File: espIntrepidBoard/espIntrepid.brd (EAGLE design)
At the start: 64 x 56 mm, 23 parts, among them Q1 TRANS_NPN, Q7 TRANS_NPN, U1 ESP32DEV_38, U2 MOSFET_P, U3 LTV-847, U5 SN65HVD233D, U6 LTV-817

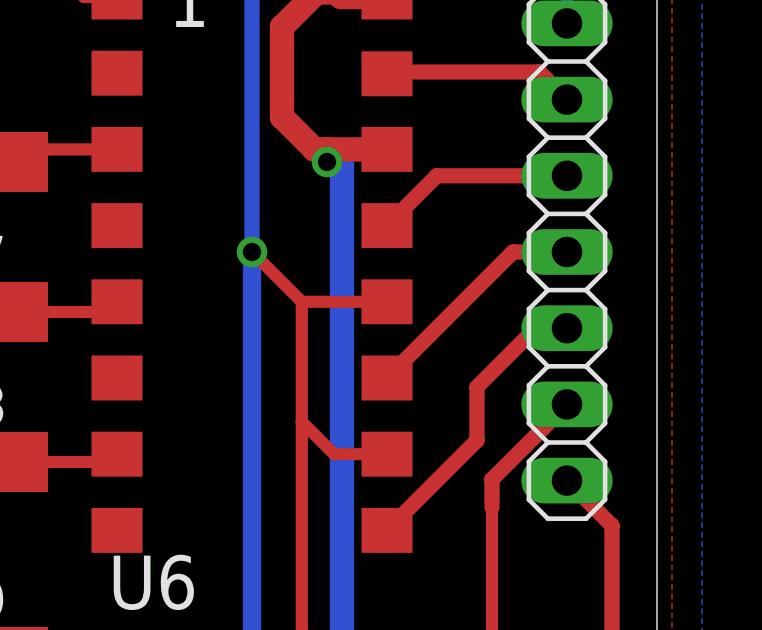
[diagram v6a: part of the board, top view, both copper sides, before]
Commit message: -Swapped 2 pins on board -Added reverse engg schematic
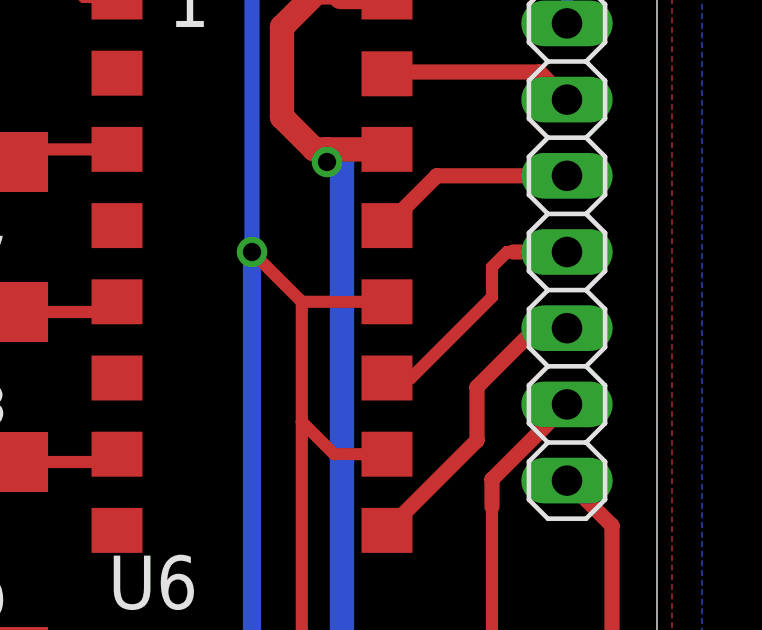
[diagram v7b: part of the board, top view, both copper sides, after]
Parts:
- Q1: value TRANS_NPN -> C1815
- R1: value (none) -> 5.6k
- R10: value (none) -> 1800
- R4: value (none) -> 5.6K
- R5, R6, R7, R8, R9: value (none) -> 470
- U2: value MOSFET_P -> DMG2307
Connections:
- net ABS: now also JP6.4, U3.11; no longer JP6.5, U3.9
- net ABS_UC: now also R7.1, U1.31; no longer R8.1, U1.30
- net AIRBAG: now also JP6.5, U3.9; no longer JP6.4, U3.11
- net AIRBAG_UC: now also R8.1, U1.30; no longer R7.1, U1.31
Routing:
- net AIRBAG: track 7.74 -> 9.87 mm
- net ABS: track 9.87 -> 8.33 mm
- net AIRBAG_UC: track 5.71 -> 6.72 mm
- net ABS_UC: track 6.72 -> 5.71 mm
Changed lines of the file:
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@@
 <attribute name="VALUE" x="41.19" y="49.725" size="1.27" layer="27"/>
 </element>
-<element name="U2" library="DR" package="SOT-23" value="MOSFET_P" x="51.5" y="47" smashed="yes" rot="R270">
+<element name="U2" library="DR" package="SOT-23" value="DMG2307" x="51.5" y="47" smashed="yes" rot="R270">
 <attribute name="NAME" x="50.2" y="48.6" size="0.6096" layer="25" rot="R270"/>
 </element>
-<element name="R1" library="DR" package="M1206" value="" x="56" y="47.5" smashed="yes">
+<element name="R1" library="DR" package="M1206" value="5.6k" x="56" y="47.5" smashed="yes">
 <attribute name="NAME" x="58.73" y="46.77" size="1.27" layer="25"/>
 <attribute name="VALUE" x="54.73" y="44.96" size="1.27" layer="27"/>
 </element>
-<element name="Q1" library="DR" package="SOT-23" value="TRANS_NPN" x="47" y="47" smashed="yes" rot="R270">
+<element name="Q1" library="DR" package="SOT-23" value="C1815" x="47" y="47" smashed="yes" rot="R270">
 <attribute name="NAME" x="45.7" y="48.6" size="0.6096" layer="25" rot="R270"/>
 </element>
-<element name="R4" library="DR" package="M1206" value="" x="41" y="48" smashed="yes">
+<element name="R4" library="DR" package="M1206" value="5.6K" x="41" y="48" smashed="yes">
 <attribute name="NAME" x="40.23" y="49.77" size="1.27" layer="25"/>
 <attribute name="VALUE" x="39.73" y="45.46" size="1.27" layer="27"/>
 </element>
-<element name="R5" library="DR" package="M1206" value="" x="41" y="44.5" smashed="yes">
+<element name="R5" library="DR" package="M1206" value="470" x="41" y="44.5" smashed="yes">
 <attribute name="NAME" x="40.23" y="41.77" size="1.27" layer="25"/>
 <attribute name="VALUE" x="39.73" y="41.96" size="1.27" layer="27"/>
 </element>
-<element name="R6" library="DR" package="M1206" value="" x="41.5" y="36.5" smashed="yes">
+<element name="R6" library="DR" package="M1206" value="470" x="41.5" y="36.5" smashed="yes">
 <attribute name="NAME" x="36.73" y="35.77" size="1.27" layer="25"/>
 <attribute name="VALUE" x="40.23" y="33.96" size="1.27" layer="27"/>
 </element>
-<element name="R7" library="DR" package="M1206" value="" x="41.5" y="31.5" smashed="yes">
+<element name="R7" library="DR" package="M1206" value="470" x="41.5" y="31.5" smashed="yes">
 <attribute name="NAME" x="40.23" y="32.77" size="1.27" layer="25"/>
 <attribute name="VALUE" x="40.23" y="28.96" size="1.27" layer="27"/>
 </element>
-<element name="R8" library="DR" package="M1206" value="" x="41.5" y="26.5" smashed="yes">
+<element name="R8" library="DR" package="M1206" value="470" x="41.5" y="26.5" smashed="yes">
 <attribute name="NAME" x="40.23" y="27.77" size="1.27" layer="25"/>
 <attribute name="VALUE" x="40.23" y="23.96" size="1.27" layer="27"/>
 </element>
-<element name="R9" library="DR" package="M1206" value="" x="41.5" y="20" smashed="yes">
+<element name="R9" library="DR" package="M1206" value="470" x="41.5" y="20" smashed="yes">
 <attribute name="NAME" x="40.23" y="21.27" size="1.27" layer="25"/>
 <attribute name="VALUE" x="40.23" y="17.46" size="1.27" layer="27"/>
@@
 <attribute name="NAME" x="46.4" y="13.7" size="0.6096" layer="25"/>
 </element>
-<element name="R10" library="DR" package="M1206" value="" x="42" y="12.5" smashed="yes">
+<element name="R10" library="DR" package="M1206" value="1800" x="42" y="12.5" smashed="yes">
 <attribute name="NAME" x="40.73" y="14.27" size="1.27" layer="25"/>
 <attribute name="VALUE" x="40.73" y="9.96" size="1.27" layer="27"/>
@@
 <wire x1="54.6" y1="47.9" x2="54.6" y2="47.5" width="0.508" layer="1"/>
 </signal>
-<signal name="ABS">
-<contactref element="U3" pad="9"/>
-<contactref element="JP6" pad="5"/>
-<wire x1="55" y1="24.22" x2="58" y2="27.22" width="0.508" layer="1"/>
-<wire x1="58" y1="29" x2="60" y2="31" width="0.508" layer="1"/>
-<wire x1="60" y1="31" x2="60.96" y2="31" width="0.508" layer="1"/>
-<wire x1="60.96" y1="31" x2="61" y2="30.96" width="0.508" layer="1"/>
-<wire x1="58" y1="27.22" x2="58" y2="29" width="0.508" layer="1"/>
-</signal>
 <signal name="OIL">
 <contactref element="U6" pad="3"/>
@@
 </signal>
 <signal name="AIRBAG">
-<contactref element="U3" pad="11"/>
-<contactref element="JP6" pad="4"/>
-<wire x1="55" y1="29.3" x2="59.2" y2="33.5" width="0.508" layer="1"/>
-<wire x1="59.2" y1="33.5" x2="61" y2="33.5" width="0.508" layer="1"/>
+<contactref element="U3" pad="9"/>
+<contactref element="JP6" pad="5"/>
+<wire x1="55" y1="24.22" x2="58" y2="27.22" width="0.508" layer="1"/>
+<wire x1="58" y1="29" x2="60" y2="31" width="0.508" layer="1"/>
+<wire x1="60" y1="31" x2="60.96" y2="31" width="0.508" layer="1"/>
+<wire x1="60.96" y1="31" x2="61" y2="30.96" width="0.508" layer="1"/>
+<wire x1="58" y1="27.22" x2="58" y2="29" width="0.508" layer="1"/>
 </signal>
 <signal name="HBEAM">
@@
 <wire x1="38.5" y1="20" x2="40.1" y2="20" width="0.4064" layer="1"/>
 </signal>
-<signal name="ABS_UC">
+<signal name="AIRBAG_UC">
 <contactref element="R8" pad="1"/>
 <contactref element="U1" pad="30"/>
@@
 <wire x1="36.42" y1="30.18" x2="40.1" y2="26.5" width="0.6096" layer="1"/>
 </signal>
-<signal name="AIRBAG_UC">
+<signal name="ABS_UC">
 <contactref element="R7" pad="1"/>
 <contactref element="U1" pad="31"/>
@@
 <wire x1="39.46" y1="7" x2="39.5" y2="6.96" width="0.4064" layer="1"/>
 </signal>
+<signal name="ABS">
+<contactref element="U3" pad="11"/>
+<contactref element="JP6" pad="4"/>
+<wire x1="59.2" y1="33.5" x2="61" y2="33.5" width="0.508" layer="1"/>
+<wire x1="55" y1="29.3" x2="55.8" y2="29.3" width="0.4064" layer="1"/>
+<wire x1="55.8" y1="29.3" x2="58.5" y2="32" width="0.4064" layer="1"/>
+<wire x1="58.5" y1="32" x2="58.5" y2="33" width="0.4064" layer="1"/>
+<wire x1="58.5" y1="33" x2="59" y2="33.5" width="0.4064" layer="1"/>
+<wire x1="59" y1="33.5" x2="59.2" y2="33.5" width="0.4064" layer="1"/>
+</signal>
 </signals>
